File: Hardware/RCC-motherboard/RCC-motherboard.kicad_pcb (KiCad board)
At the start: 2 copper layers, 26 parts, among them J1 1760510000, J2 1760510000, J3 1760510000, J4 1760510000, J5 1760510000, U1 ESP32-DEVKITC-32D, U2 DMG3415U-7, U3 TB6612FNG, U4 TB6612FNG, U5 ZLDO1117G33TA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

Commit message: Finished PCB Layout
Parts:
- moved C1 6.83 mm to (170.1, 110.0)
- moved C2 6.48 mm to (172.2, 109.9)
- moved C10 4.96 mm to (133.2, 123.2)
- moved C4 4.96 mm to (145.1, 77.8)
- moved C7 4.96 mm to (132.1, 79.8)
- moved J2 4.96 mm to (172.3, 101.8)
- moved J3 4.96 mm to (132.1, 96.7)
- moved J4 4.96 mm to (132.1, 130.8)
- moved J5 4.96 mm to (154.4, 78.6)
- moved U1 4.96 mm to (152.1, 111.8)
- moved U3 4.96 mm to (171.7, 117.0)
- moved U5 4.96 mm to (139.1, 79.8)
- moved C11 4.96 mm to (135.2, 124.2)
- moved U2 4.96 mm to (131.1, 87.7)
- moved J1 4.96 mm to (172.3, 135.9)
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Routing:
- net +3V3: track 30.5 -> 155.1 mm, vias 0 -> 10
- net +5V: track 58.3 -> 11.8 mm, vias 2 -> 0
- net GND: track 37.2 -> 74.2 mm, vias 9 -> 14
- net AIN1_M1: track 0.00 -> 34.3 mm
- net PWM_A_M1: track 0.00 -> 30.7 mm, vias 0 -> 2
- net BO2_M1: track 0.00 -> 25.5 mm
- net STBY_M2: track 0.00 -> 23.9 mm, vias 0 -> 2
- net PWM_B_M1: track 0.00 -> 23.1 mm
- net BO2_M2: track 0.65 -> 21.8 mm
- net AIN2_M1: track 0.00 -> 20.9 mm, vias 0 -> 2
- net AO1_M1: track 0.00 -> 18.8 mm
- net STBY_M1: track 0.00 -> 17.9 mm
- net AO1_M2: track 0.65 -> 18.5 mm
- net AO2_M2: track 0.65 -> 18.3 mm, vias 0 -> 2
- net AO2_M1: track 0.00 -> 16.6 mm
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- added copper zone on F.Cu, net +5V
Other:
- board outline added: 53.3 x 66 mm

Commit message: Produced Gerber and Production files
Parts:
- added H1: MountingHole_3.2mm_M3_ISO7380, MountingHole:MountingHole_3.2mm_M3_ISO7380, F.Cu at (152.1, 106.7)
- U5: value ZLDO1117G33TA -> AZ1117IH-3.3TRG1; footprint SnapEDA Library:SOT230P700X180-4N -> SnapEDA Library:SOT230P700X185-4N
- moved J5 0.85 mm to (155.2, 78.6)
- moved J3 0.75 mm to (132.8, 96.7)
- moved J4 0.75 mm to (132.8, 130.8)
- moved U6 0.59 mm to (173.2, 84.6)
- moved C6 0.48 mm to (162.4, 81.8)
- moved J1 0.25 mm to (172.5, 135.9)
- moved J2 0.25 mm to (172.5, 101.8)
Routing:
- net +5V: track 11.8 -> 2.63 mm
- net GND: track 74.2 -> 75.4 mm
- net Vin: track 34.3 -> 35.1 mm
- net AO2_M2: track 18.3 -> 18.8 mm
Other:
- board text added: "Ameen AlShaibani BLE Motor Control Board 2023"
- board text added: "JLCJLCJLCJLC"
- board text added: "M1"
- board text added: "M2"
- board text added: "M3"
- board text added: "M4"
- board text added: "Motor Ratings: Voltage: 5V Max Current: 1.2A"
- board text added: "PWR IN 5V - 12V"
- board text removed: "each motor stalls at 1.2A, thus for 4 motors I need around 5 A, My 5v buck converter can provide upto 3A, and the motor drivers can provide upto 1.2A to each motor and upto 3A for short bursts. How much current should I design my traces to handle?"

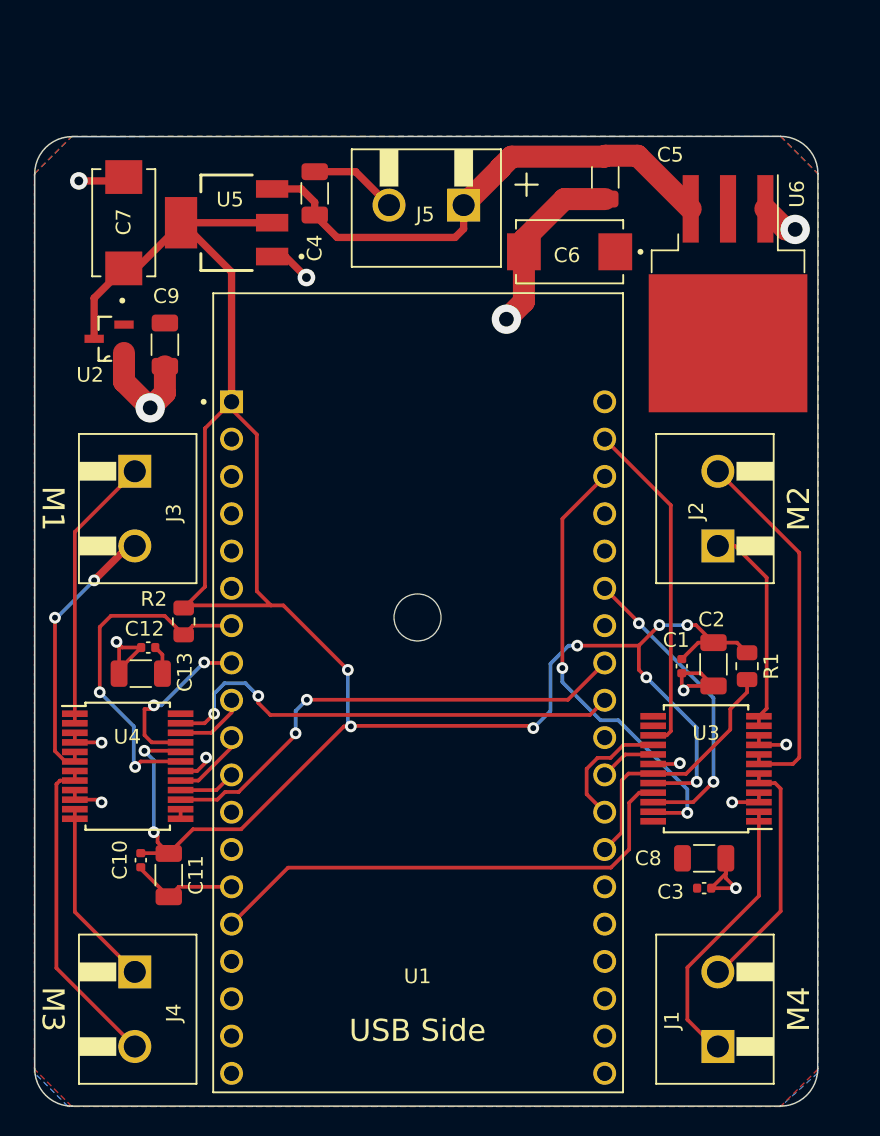
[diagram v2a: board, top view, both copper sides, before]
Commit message: Size standarized to mm, and board is ordered
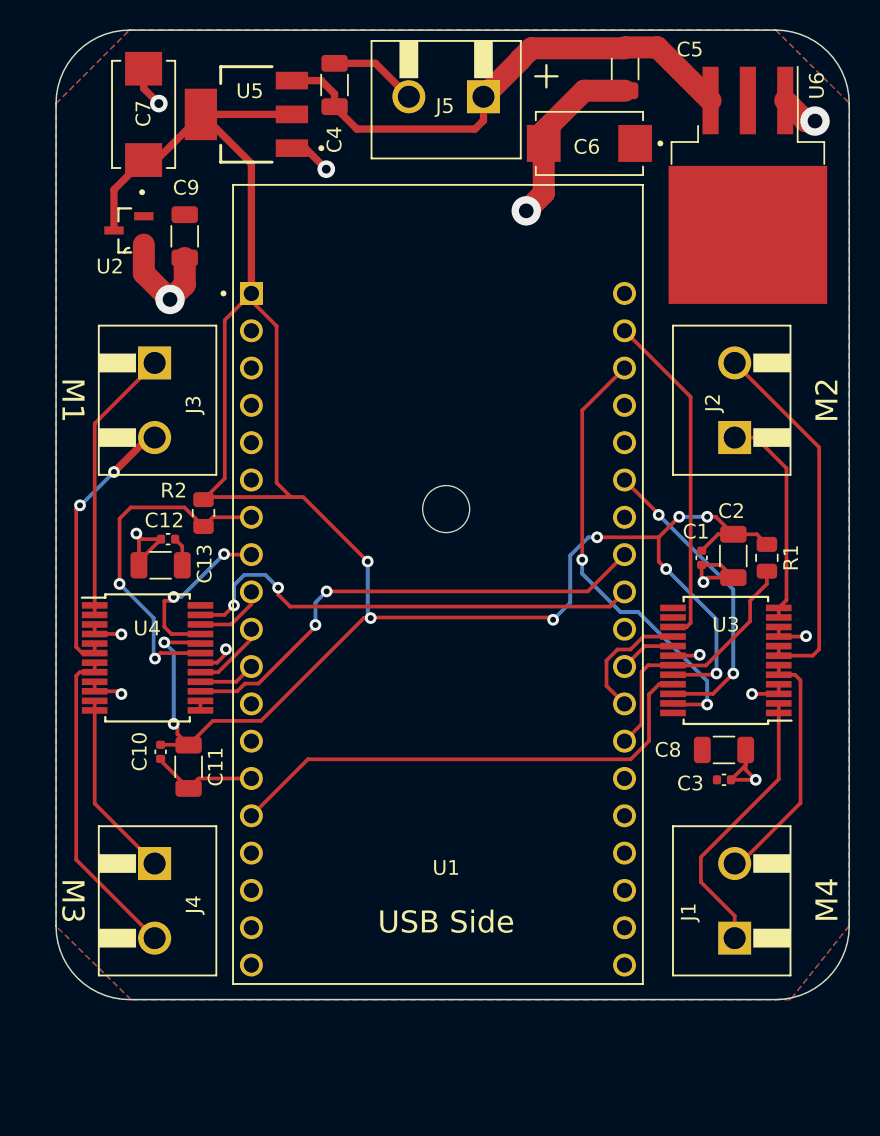
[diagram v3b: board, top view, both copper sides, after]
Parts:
- moved H1 7.63 mm to (154.0, 99.3)
- moved C1 7.50 mm to (171.4, 102.6)
- moved C3 7.50 mm to (173.0, 117.7)
- moved C5 7.50 mm to (166.2, 69.3)
- moved J3 7.50 mm to (134.2, 89.4)
- moved J4 7.50 mm to (134.2, 123.4)
- moved R2 7.50 mm to (137.5, 99.6)
- moved U3 7.50 mm to (173.1, 109.6)
- moved U4 7.50 mm to (133.7, 109.4)
- moved C10 7.50 mm to (134.6, 115.8)
- moved C4 7.50 mm to (146.4, 70.4)
- moved C7 7.50 mm to (133.4, 72.4)
- moved R1 7.50 mm to (175.9, 102.6)
- moved U1 7.50 mm to (153.5, 104.4)
- moved U5 7.50 mm to (140.4, 72.4)
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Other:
- board size 53.3 x 66 mm -> 54 x 66 mm

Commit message: Board uses ESP32-DEVKITC not narrow version
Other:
- board text added: "THE FOOTPRINT IS WRONG"
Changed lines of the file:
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@@
     )
     (pad_to_mask_clearance 0)
-    (grid_origin 132.48 66.696051)
     (pcbplotparams
       (layerselection 0x00010fc_ffffffff)
@@
     (effects (font (size 1.5 1.5) (thickness 0.15)))
   )
+  (gr_text "THE FOOTPRINT IS WRONG" (at 153.7 92.4) (layer "Dwgs.User")
+    (effects (font (size 1 1) (thickness 0.25)))
+  )
   (dimension (type orthogonal) (layer "Dwgs.User")
